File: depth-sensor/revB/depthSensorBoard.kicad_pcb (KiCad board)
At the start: 2 copper layers, 66.5 x 44.5 mm, 43 parts, among them IC1 ATMEGA1284P-M, P1 Mezzanine-Header, P10 Spacer, P2 CONN_02X03, P3 CONN_01X04, P4 CONN_01X04, P5 CONN_01X04, P6 CONN_01X04, P7 Spacer, P8 Spacer, P9 Spacer, Q1 Q_PMOS_GSD, U1 AP2112, U2 TCA9545A, U3 TSX-3225

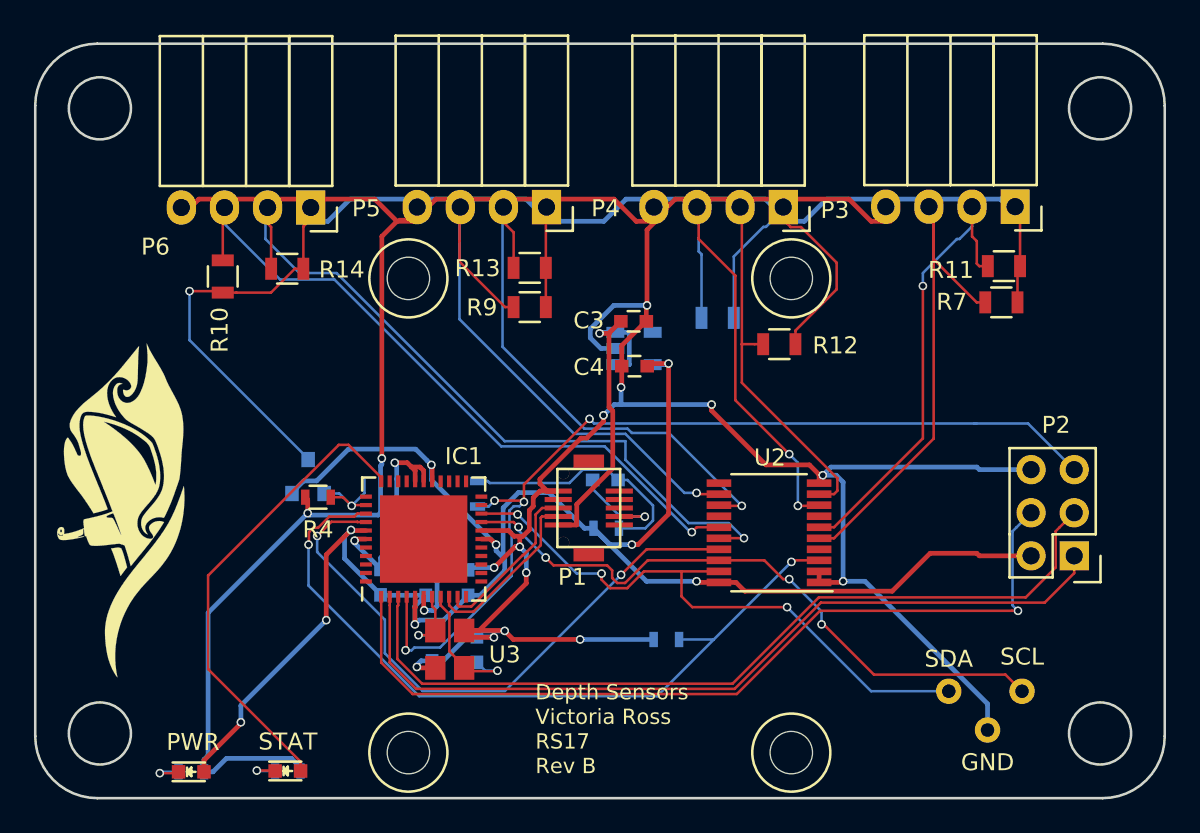
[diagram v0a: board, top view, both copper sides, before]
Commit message: converted edge-cut mounting holes to KiCAD components
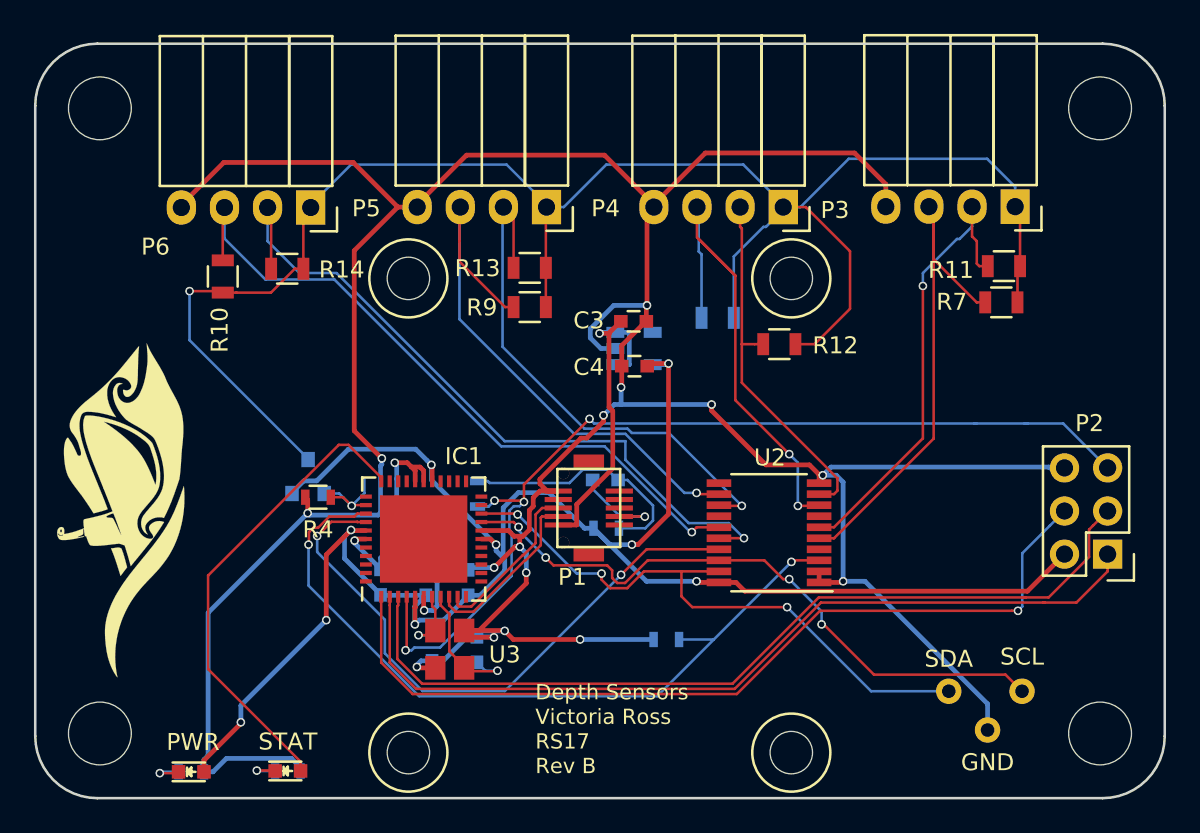
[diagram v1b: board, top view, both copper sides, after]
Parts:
- added REF**: MountingHole_3.7mm, Mounting_Holes:MountingHole_3.7mm, F.Cu at (101.2, 113.4)
- added REF**: MountingHole_3.7mm, Mounting_Holes:MountingHole_3.7mm, F.Cu at (160.1, 113.4)
- added REF**: MountingHole_3.7mm, Mounting_Holes:MountingHole_3.7mm, F.Cu at (160.1, 76.5)
- added REF**: MountingHole_3.7mm, Mounting_Holes:MountingHole_3.7mm, F.Cu at (101.2, 76.5)
- moved P2 1.97 mm to (160.5, 102.8)
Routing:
- net GND: track 231.3 -> 239.8 mm
- net /depth_power: track 97.2 -> 104.7 mm
- net /SDA1: track 26.3 -> 30.1 mm
- net /ATMega1284p/~RST: track 55.5 -> 57.7 mm
- net /ATMega1284p/MISO: track 48.7 -> 50.8 mm
- net /ATMega1284p/SCK: track 49.6 -> 51.5 mm
- net +3V3: track 110.9 -> 112.8 mm
- net /SDA3: track 39.6 -> 41.4 mm
- net /SCL3: track 41.7 -> 43.1 mm
- net /SCL2: track 30.0 -> 30.8 mm
- net /SCL1: track 20.8 -> 21.5 mm
- net /ATMega1284p/MOSI: track 50.6 -> 51.2 mm
- net (no net): track 0.61 -> 0.00 mm
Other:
- outline, holes or cut-outs redrawn
